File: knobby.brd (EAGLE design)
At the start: 74.6 x 74.9 mm, 20 parts

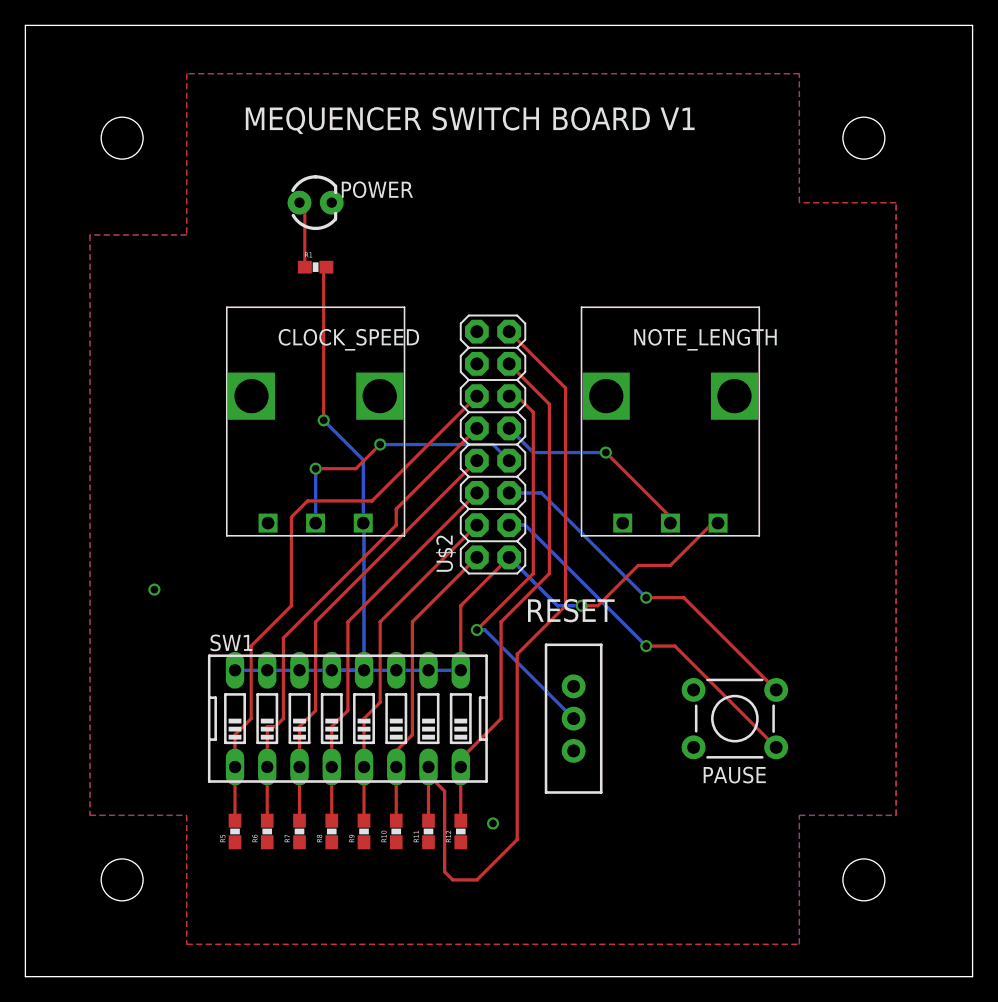
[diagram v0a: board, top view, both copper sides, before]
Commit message: Knobby board layed out with 4 jacks
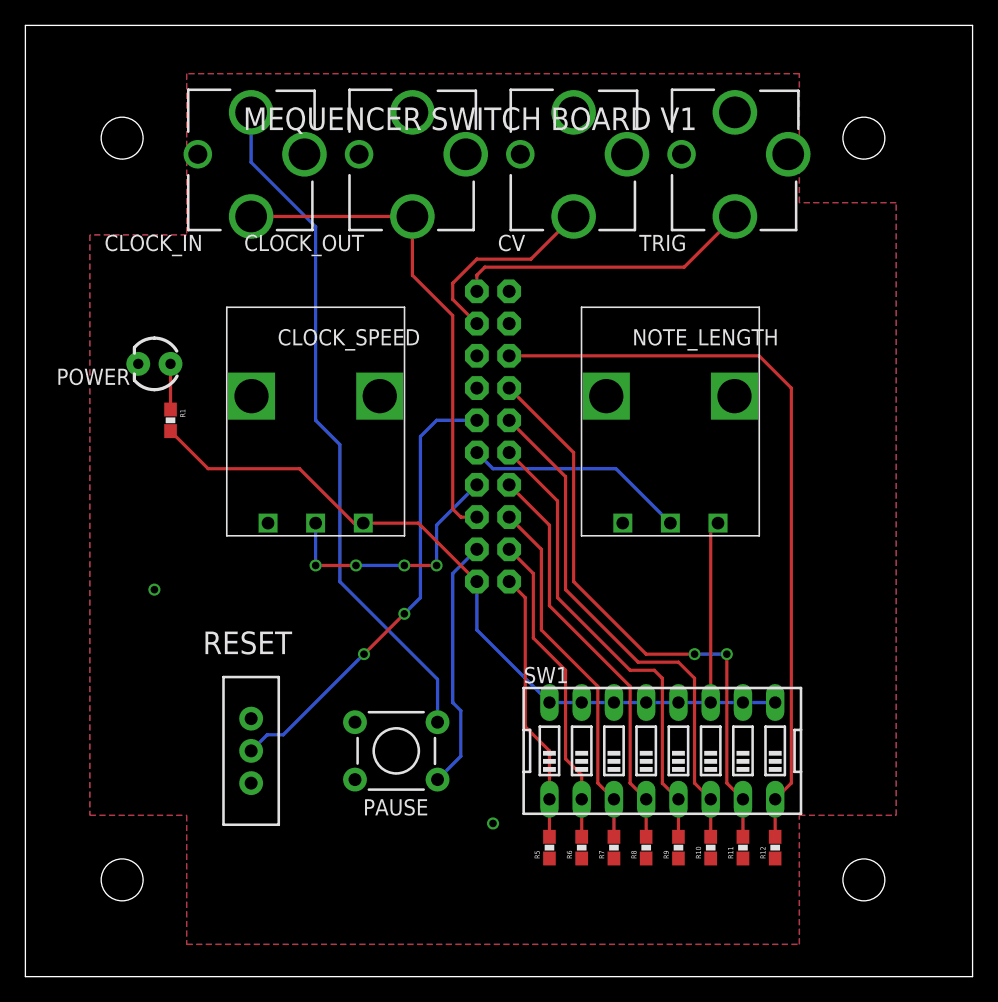
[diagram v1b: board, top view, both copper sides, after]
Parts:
- added CLOCK_IN, CLOCK_OUT, CV, TRIG: AUDIO-JACKERTHENVAR, erthenvar:ERTHENVAR-JACK
- U$2: value M08X2 -> M10X2; device SparkFun-Connectors:2X8 -> SparkFun-Connectors:2X10
- moved PAUSE 26.8 mm to (29.2, 17.8)
- moved RESET 25.5 mm to (17.8, 17.8)
- moved SW1 24.9 mm to (50.2, 17.8)
- moved R8 24.8 mm to (48.9, 10.2)
- moved R10 24.8 mm to (54.0, 10.2)
- moved R11 24.8 mm to (56.5, 10.2)
- moved R12 24.8 mm to (59.1, 10.2)
- moved R9 24.8 mm to (51.4, 10.2)
- moved R5 24.8 mm to (41.3, 10.2)
- moved R6 24.8 mm to (43.8, 10.2)
- moved R7 24.8 mm to (46.4, 10.2)
- moved POWER 18.0 mm to (10.2, 48.3), turned to 180 degrees
- moved R1 16.6 mm to (11.4, 43.8), turned to 270 degrees
- moved U$2 9.61 mm to (36.8, 42.5), flipped to the bottom
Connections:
- net PAUSE_IN renamed INT_CLOCK
- removed net N$16: U$2.14
- new net CLOCK: CLOCK_IN.3, CLOCK_OUT.3, U$2.5
- new net CV: CV.3, U$2.17
- new net TRIG: TRIG.3, U$2.19
- net GND: now also CLOCK_IN.1@1, CLOCK_IN.1@2, CLOCK_OUT.1@1, CLOCK_OUT.1@2, CV.1@1, CV.1@2, TRIG.1@1, TRIG.1@2, U$2.20; no longer U$2.16
- net LOAD0: now also U$2.8; no longer U$2.6
- net LOAD1: now also U$2.6; no longer U$2.8
- net LOAD2: now also U$2.4; no longer U$2.10
- net LOAD3: now also U$2.2; no longer U$2.12
- net PAUSE_OUT: now also CLOCK_IN.2; no longer U$2.5
- net RESET0: now also U$2.16; no longer U$2.13
- net RESET1: now also U$2.14; no longer U$2.15
- net RESET2: now also U$2.12; no longer U$2.2
- net RESET3: now also U$2.10; no longer U$2.4
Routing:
- net CLOCK: track 0.00 -> 39.2 mm
- net PAUSE_OUT: track 27.5 -> 54.1 mm, vias 1 -> 0
- net TRIG: track 0.00 -> 23.5 mm
- net LOAD3: track 44.3 -> 21.4 mm
- net RESET0: track 40.2 -> 59.1 mm
- net RESET2: track 23.4 -> 41.2 mm
- net RESET1: track 63.7 -> 46.7 mm, vias 0 -> 2
- net CV: track 0.00 -> 15.7 mm
- net LOAD2: track 38.1 -> 25.0 mm
- net 5V: track 85.8 -> 73.1 mm, vias 2 -> 0
- net RESET3: track 27.0 -> 36.9 mm
- net INT_CLOCK: track 28.3 -> 19.9 mm, vias 1 -> 0
- net LOAD1: track 34.1 -> 28.6 mm
- net LOAD: track 31.9 -> 36.0 mm, vias 1 -> 2
- net N$1: track 5.25 -> 3.59 mm
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
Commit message: Moving shit around
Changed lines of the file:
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@@
 <wire x1="74.6" y1="74.92" x2="0" y2="74.92" width="0" layer="20"/>
 <wire x1="0" y1="74.92" x2="0" y2="0" width="0" layer="20"/>
-<text x="17.145" y="66.675" size="1.778" layer="25">MEQUENCER SWITCH BOARD V1</text>
+<text x="17.78" y="71.755" size="1.778" layer="25">MEQUENCER SWITCH BOARD V1</text>
 </plain>
 <attributes>

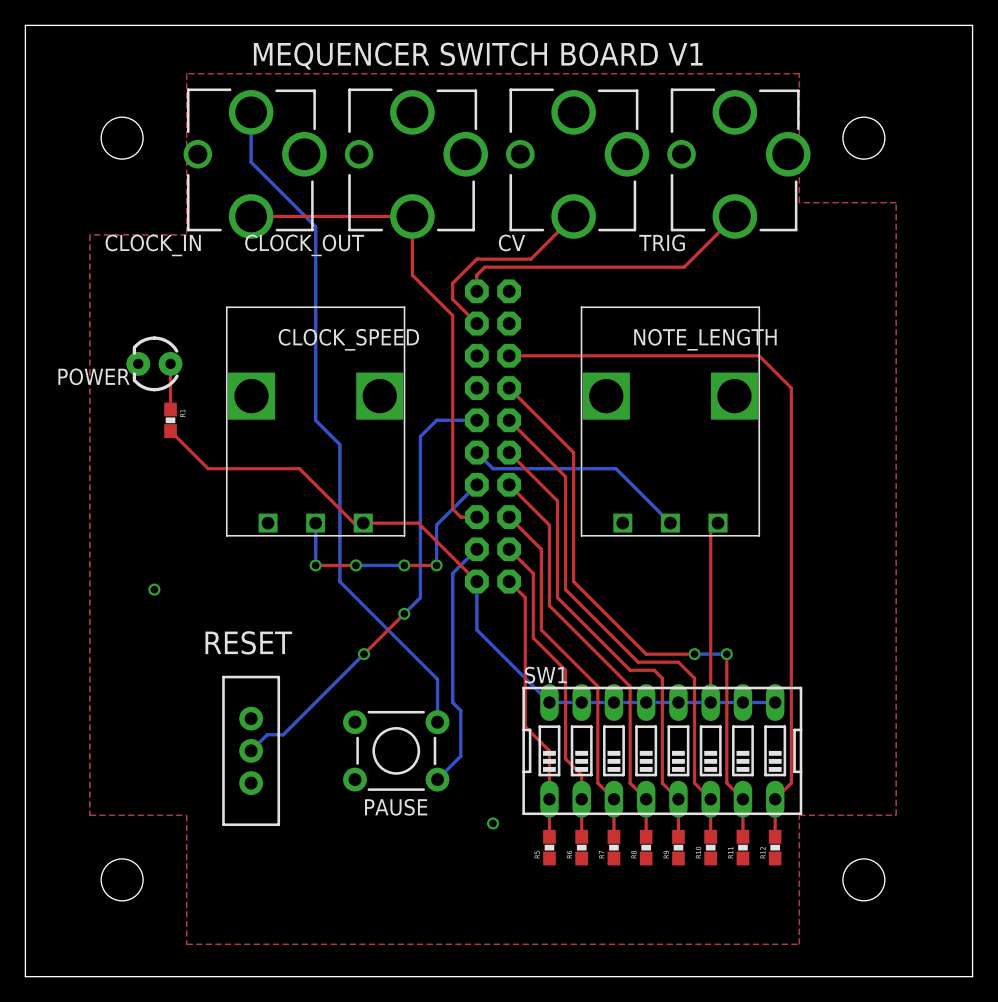
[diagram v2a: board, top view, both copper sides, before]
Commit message: test points and jack resistors
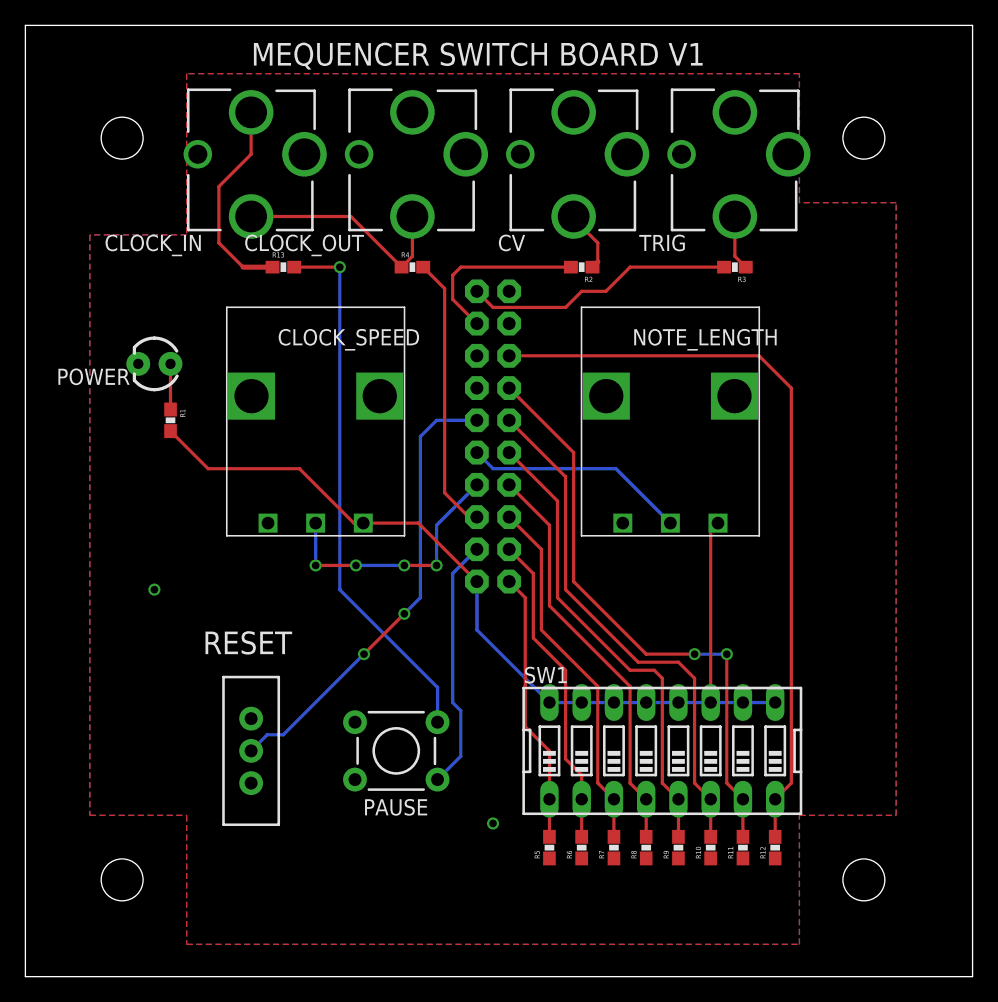
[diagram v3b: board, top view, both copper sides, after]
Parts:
- added R13, R2, R3, R4: 10k, SparkFun-Resistors:0603-RES
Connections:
- new net N$2: CV.3, R2.1
- new net N$3: R3.1, TRIG.3
- new net N$4: CLOCK_IN.3, CLOCK_OUT.3, R4.1
- new net N$5: CLOCK_IN.2, R13.1
- net CLOCK: now also R4.2; no longer CLOCK_IN.3, CLOCK_OUT.3
- net CV: now also R2.2; no longer CV.3
- net PAUSE_OUT: now also R13.2; no longer CLOCK_IN.2
- net TRIG: now also R3.2; no longer TRIG.3
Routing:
- net N$4: track 0.00 -> 17.8 mm
- net CLOCK: track 39.2 -> 21.8 mm
- net N$5: track 0.00 -> 16.4 mm
- net PAUSE_OUT: track 54.1 -> 42.6 mm, vias 0 -> 1
- net N$2: track 0.00 -> 4.95 mm
- net N$3: track 0.00 -> 4.34 mm
- net TRIG: track 23.5 -> 21.3 mm
- net CV: track 15.7 -> 14.2 mm
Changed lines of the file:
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@@
 <?xml version="1.0" encoding="utf-8"?>
 <!DOCTYPE eagle SYSTEM "eagle.dtd">
-<eagle version="6.4">
+<eagle version="6.5.0">
 <drawing>
 <settings>
@@
 <element name="CV" library="erthenvar" package="ERTHENVAR-JACK" value="AUDIO-JACKERTHENVAR" x="43.18" y="64.77" rot="R180"/>
 <element name="TRIG" library="erthenvar" package="ERTHENVAR-JACK" value="AUDIO-JACKERTHENVAR" x="55.88" y="64.77" rot="R180"/>
+<element name="R2" library="SparkFun-Resistors" package="0603-RES" value="10k" x="43.815" y="55.88" rot="R180"/>
+<element name="R3" library="SparkFun-Resistors" package="0603-RES" value="10k" x="55.88" y="55.88" rot="R180"/>
+<element name="R4" library="SparkFun-Resistors" package="0603-RES" value="10k" x="30.48" y="55.88"/>
+<element name="R13" library="SparkFun-Resistors" package="0603-RES" value="10k" x="20.32" y="55.88"/>
 </elements>
 <signals>
@@
 <signal name="PAUSE_OUT">
 <contactref element="PAUSE" pad="3"/>
-<contactref element="CLOCK_IN" pad="2"/>
-<wire x1="32.4612" y1="20.0406" x2="32.4612" y2="23.4188" width="0.254" layer="16"/>
-<wire x1="32.4612" y1="23.4188" x2="24.765" y2="31.115" width="0.254" layer="16"/>
-<wire x1="24.765" y1="31.115" x2="24.765" y2="41.91" width="0.254" layer="16"/>
-<wire x1="24.765" y1="41.91" x2="22.86" y2="43.815" width="0.254" layer="16"/>
-<wire x1="22.86" y1="43.815" x2="22.86" y2="59.055" width="0.254" layer="16"/>
-<wire x1="22.86" y1="59.055" x2="17.78" y2="64.135" width="0.254" layer="16"/>
-<wire x1="17.78" y1="64.135" x2="17.78" y2="68.07" width="0.254" layer="16"/>
+<contactref element="R13" pad="2"/>
+<wire x1="32.4612" y1="20.0406" x2="32.4612" y2="22.7838" width="0.254" layer="16"/>
+<wire x1="32.4612" y1="22.7838" x2="24.765" y2="30.48" width="0.254" layer="16"/>
+<wire x1="24.765" y1="30.48" x2="24.765" y2="55.88" width="0.254" layer="16"/>
+<via x="24.765" y="55.88" extent="1-16" drill="0.6"/>
+<wire x1="24.765" y1="55.88" x2="21.17" y2="55.88" width="0.254" layer="1"/>
 </signal>
 <signal name="LOAD">
@@
 </signal>
 <signal name="CV">
-<contactref element="CV" pad="3"/>
 <contactref element="U$2" pad="17"/>
-<wire x1="35.56" y1="51.435" x2="33.655" y2="53.34" width="0.254" layer="1"/>
-<wire x1="33.655" y1="53.34" x2="33.655" y2="54.61" width="0.254" layer="1"/>
-<wire x1="33.655" y1="54.61" x2="35.56" y2="56.515" width="0.254" layer="1"/>
-<wire x1="35.56" y1="56.515" x2="39.825" y2="56.515" width="0.254" layer="1"/>
-<wire x1="39.825" y1="56.515" x2="43.18" y2="59.87" width="0.254" layer="1"/>
+<contactref element="R2" pad="2"/>
+<wire x1="42.965" y1="55.88" x2="34.29" y2="55.88" width="0.254" layer="1"/>
+<wire x1="34.29" y1="55.88" x2="33.655" y2="55.245" width="0.254" layer="1"/>
+<wire x1="33.655" y1="55.245" x2="33.655" y2="53.34" width="0.254" layer="1"/>
+<wire x1="33.655" y1="53.34" x2="35.56" y2="51.435" width="0.254" layer="1"/>
 </signal>
 <signal name="N$1">
@@
 </signal>
 <signal name="CLOCK">
-<contactref element="CLOCK_IN" pad="3"/>
-<contactref element="CLOCK_OUT" pad="3"/>
 <contactref element="U$2" pad="5"/>
-<wire x1="17.78" y1="59.87" x2="30.48" y2="59.87" width="0.254" layer="1"/>
-<wire x1="35.56" y1="36.195" x2="34.29" y2="36.195" width="0.254" layer="1"/>
-<wire x1="34.29" y1="36.195" x2="33.655" y2="36.83" width="0.254" layer="1"/>
-<wire x1="33.655" y1="36.83" x2="33.655" y2="52.07" width="0.254" layer="1"/>
-<wire x1="33.655" y1="52.07" x2="30.48" y2="55.245" width="0.254" layer="1"/>
-<wire x1="30.48" y1="55.245" x2="30.48" y2="59.87" width="0.254" layer="1"/>
+<contactref element="R4" pad="2"/>
+<wire x1="35.56" y1="36.195" x2="34.925" y2="36.195" width="0.4064" layer="1"/>
+<wire x1="34.925" y1="36.195" x2="33.02" y2="38.1" width="0.254" layer="1"/>
+<wire x1="33.02" y1="38.1" x2="33.02" y2="54.19" width="0.254" layer="1"/>
+<wire x1="33.02" y1="54.19" x2="31.33" y2="55.88" width="0.254" layer="1"/>
 </signal>
 <signal name="INT_CLOCK">
@@
 </signal>
 <signal name="TRIG">
+<contactref element="U$2" pad="19"/>
+<contactref element="R3" pad="2"/>
+<wire x1="55.03" y1="55.88" x2="47.625" y2="55.88" width="0.254" layer="1"/>
+<wire x1="47.625" y1="55.88" x2="45.72" y2="53.975" width="0.254" layer="1"/>
+<wire x1="45.72" y1="53.975" x2="43.815" y2="53.975" width="0.254" layer="1"/>
+<wire x1="43.815" y1="53.975" x2="42.545" y2="52.705" width="0.254" layer="1"/>
+<wire x1="42.545" y1="52.705" x2="36.83" y2="52.705" width="0.254" layer="1"/>
+<wire x1="36.83" y1="52.705" x2="35.56" y2="53.975" width="0.254" layer="1"/>
+</signal>
+<signal name="N$2">
+<contactref element="R2" pad="1"/>
+<contactref element="CV" pad="3"/>
+<wire x1="43.18" y1="59.87" x2="43.18" y2="59.69" width="0.254" layer="1"/>
+<wire x1="43.18" y1="59.69" x2="45.085" y2="57.785" width="0.254" layer="1"/>
+<wire x1="45.085" y1="57.785" x2="45.085" y2="56.3" width="0.254" layer="1"/>
+<wire x1="45.085" y1="56.3" x2="44.665" y2="55.88" width="0.4064" layer="1"/>
+</signal>
+<signal name="N$3">
 <contactref element="TRIG" pad="3"/>
-<contactref element="U$2" pad="19"/>
-<wire x1="35.56" y1="53.975" x2="35.56" y2="55.245" width="0.254" layer="1"/>
-<wire x1="35.56" y1="55.245" x2="36.195" y2="55.88" width="0.254" layer="1"/>
-<wire x1="36.195" y1="55.88" x2="51.89" y2="55.88" width="0.254" layer="1"/>
-<wire x1="51.89" y1="55.88" x2="55.88" y2="59.87" width="0.254" layer="1"/>
+<contactref element="R3" pad="1"/>
+<wire x1="55.88" y1="59.87" x2="55.88" y2="56.73" width="0.254" layer="1"/>
+<wire x1="55.88" y1="56.73" x2="56.73" y2="55.88" width="0.254" layer="1"/>
+</signal>
+<signal name="N$4">
+<contactref element="CLOCK_IN" pad="3"/>
+<contactref element="CLOCK_OUT" pad="3"/>
+<contactref element="R4" pad="1"/>
+<wire x1="30.48" y1="59.87" x2="30.48" y2="56.73" width="0.254" layer="1"/>
+<wire x1="30.48" y1="56.73" x2="29.63" y2="55.88" width="0.254" layer="1"/>
+<wire x1="17.78" y1="59.87" x2="25.64" y2="59.87" width="0.254" layer="1"/>
+<wire x1="25.64" y1="59.87" x2="29.63" y2="55.88" width="0.254" layer="1"/>
+</signal>
+<signal name="N$5">
+<contactref element="CLOCK_IN" pad="2"/>
+<contactref element="R13" pad="1"/>
+<wire x1="17.78" y1="68.07" x2="17.78" y2="64.77" width="0.254" layer="1"/>
+<wire x1="17.78" y1="64.77" x2="15.24" y2="62.23" width="0.254" layer="1"/>
+<wire x1="15.24" y1="62.23" x2="15.24" y2="57.785" width="0.254" layer="1"/>
+<wire x1="15.24" y1="57.785" x2="17.145" y2="55.88" width="0.254" layer="1"/>
+<wire x1="17.145" y1="55.88" x2="19.47" y2="55.88" width="0.4064" layer="1"/>
 </signal>
 </signals>
